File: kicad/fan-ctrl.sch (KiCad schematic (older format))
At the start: 22 parts

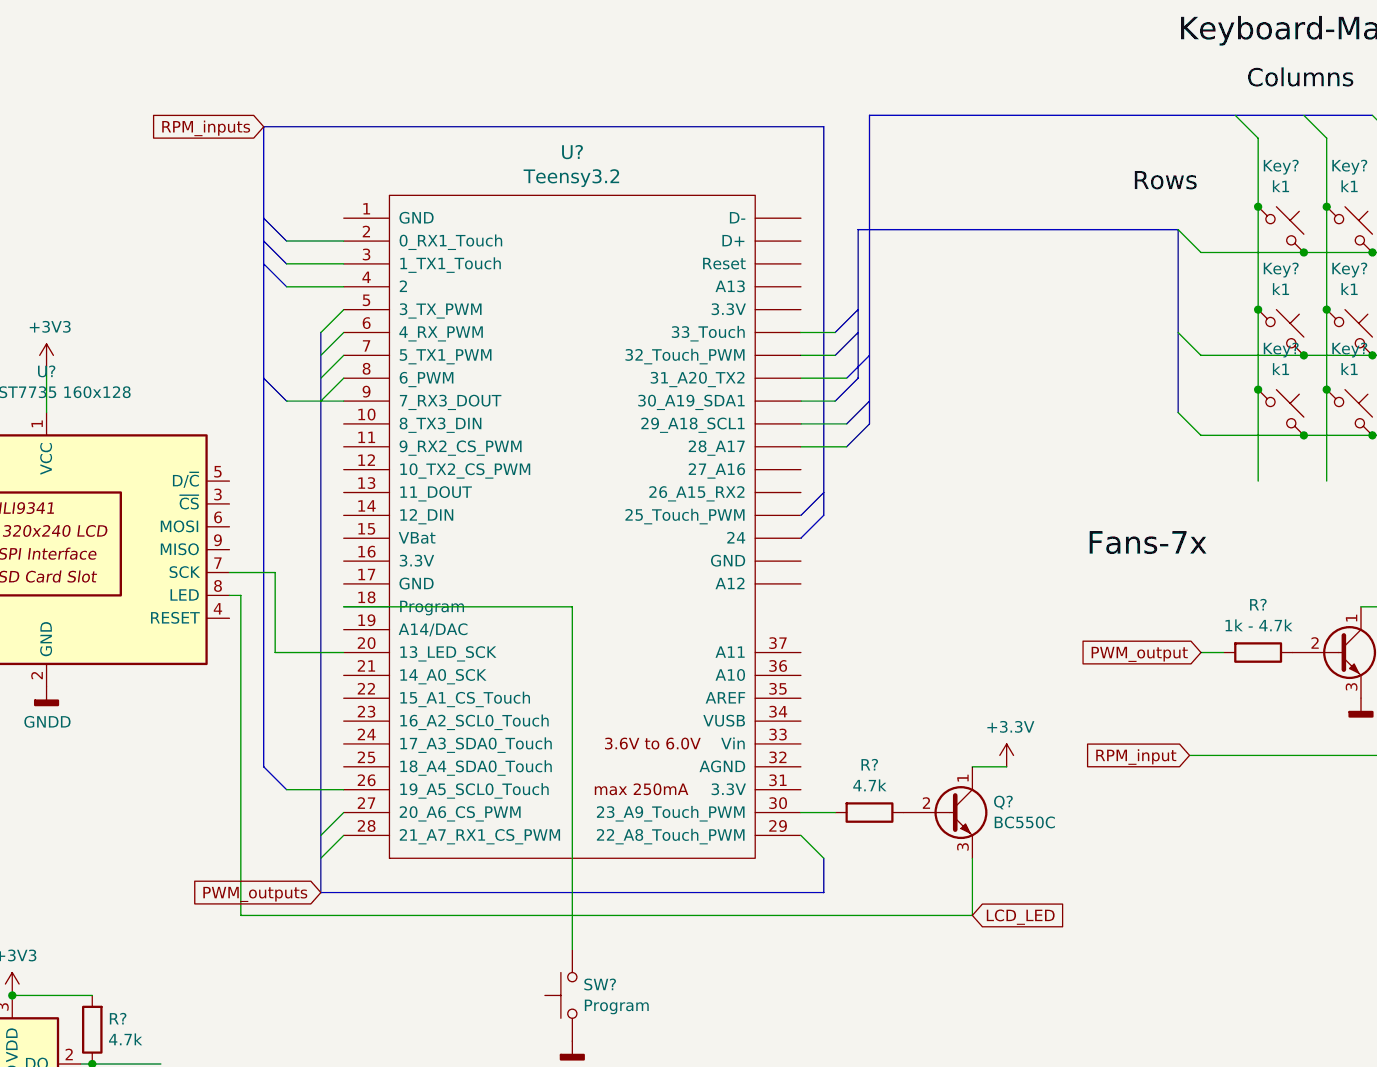
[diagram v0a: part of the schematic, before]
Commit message: many DS18B20, no adc thermocouples
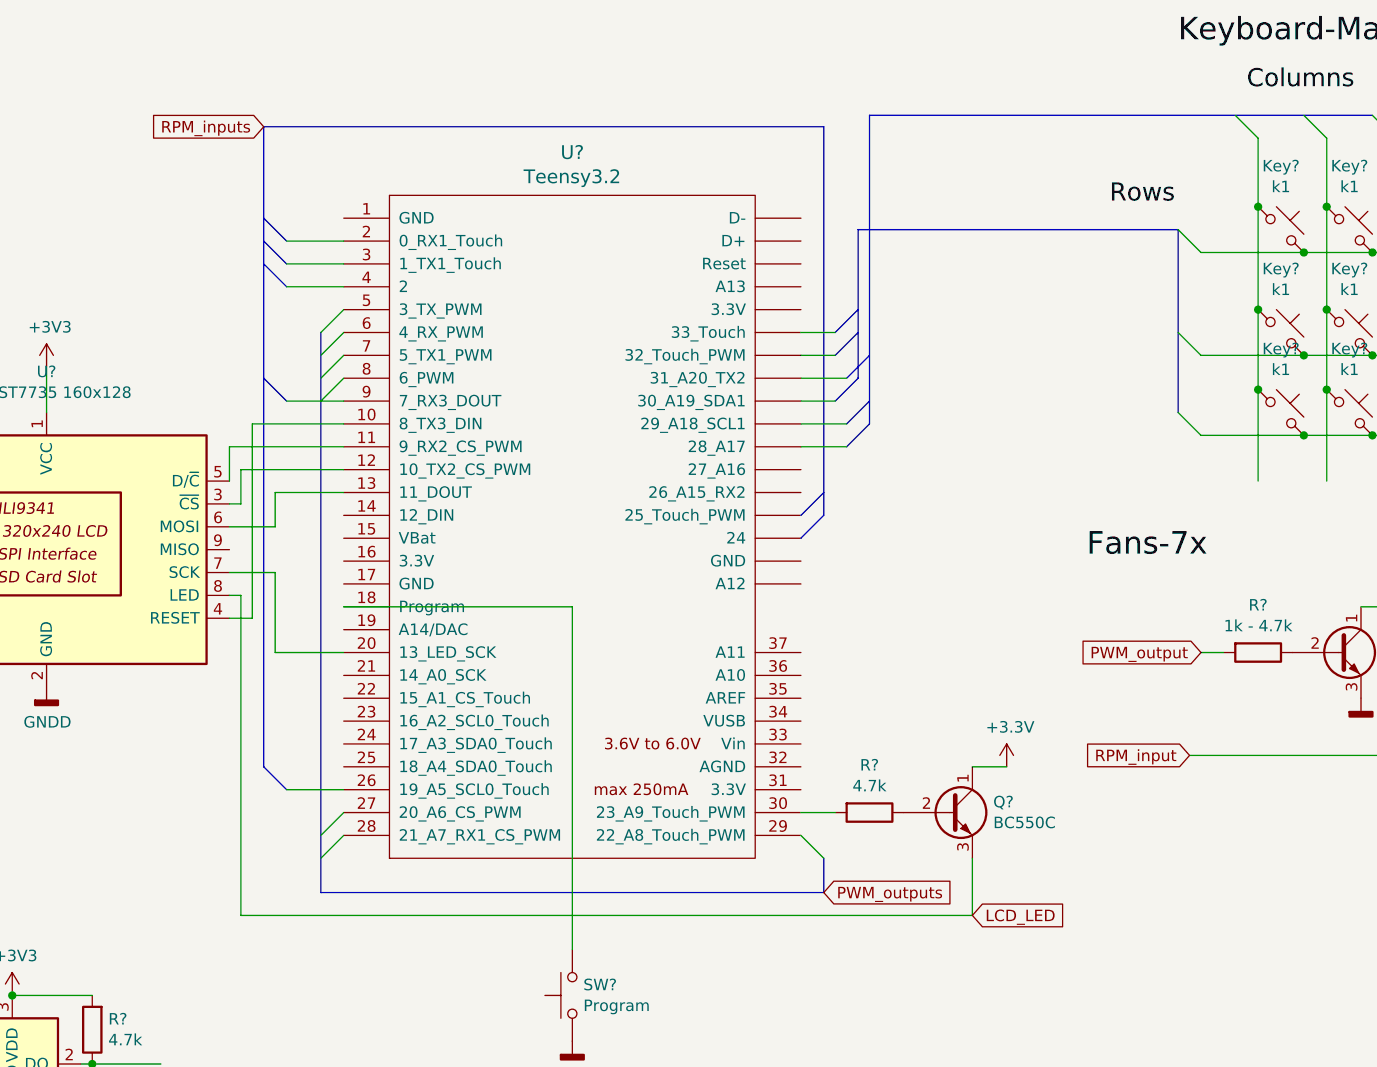
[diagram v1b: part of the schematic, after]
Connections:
- wire segments 57 -> 68
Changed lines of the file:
@@
 Wire Bus Line
 	4700 4700 2500 4700
-Text GLabel 2500 4700 0    50   Input ~ 0
+Text GLabel 4700 4700 2    50   Input ~ 0
 PWM_outputs
 Text GLabel 5350 4800 2    50   Input ~ 0
@@
 Text Label 6550 1200 0    79   ~ 0
 Columns
-Text Label 6050 1650 0    79   ~ 0
+Text Label 5950 1700 0    79   ~ 0
 Rows
 Text Label 6250 1000 0    98   ~ 0
@@
 Wire Wire Line
 	7400 2700 7600 2700
+Wire Wire Line
+	2600 2850 2150 2850
+Wire Wire Line
+	2150 2850 2150 3000
+Wire Wire Line
+	2150 3000 2100 3000
+Wire Wire Line
+	2600 2650 2200 2650
+Wire Wire Line
+	2200 2650 2200 3500
+Wire Wire Line
+	2200 3500 2100 3500
+Wire Wire Line
+	2600 2750 2100 2750
+Wire Wire Line
+	2100 2750 2100 2900
+Wire Wire Line
+	2600 2950 2300 2950
+Wire Wire Line
+	2300 2950 2300 3100
+Wire Wire Line
+	2300 3100 2100 3100
 Wire Bus Line
 	6250 1800 6250 2600

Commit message: schematics upd
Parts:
- removed R?: 4.7k, symbol Device:R
- added C? (x2): 1000u, symbol Device:CP
- added C? (x3): 100n, symbol Device:C
- added C?: 470u, symbol Device:CP
- added C?: 470n, symbol Device:C
- added M? (x2): Fan, symbol Motor:Fan_Tacho
- added Q? (x2): BD140, Package_TO_SOT_THT:TO-126-3_Vertical, symbol Transistor_BJT:BD140
- added Q? (x2): BC550C, Package_TO_SOT_THT:TO-92_Inline, symbol Transistor_BJT:BC550
- added R? (x3): 4.7k, symbol Device:R
- added R? (x3): 1k, symbol Device:R
- added R?: 100, symbol Device:R
- added U? (x2): (no value), Package_TO_SOT_THT:TO-92_Inline, symbol Sensor_Temperature:DS18B20
- M?: value Fan_Tacho -> Fan PWM
- R?: value 1k - 4.7k -> 4.7k
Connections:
- net labels added: FAN_output, FAN_outputs, Fans-Analog, Fans-PWM, High-Power, Temperature-sensors
- net labels removed: Fans-7x, PWM_output, PWM_outputs
- wire segments 68 -> 101
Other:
- moved on the sheet: C?, Key?, M?, Q?, R?, U?
